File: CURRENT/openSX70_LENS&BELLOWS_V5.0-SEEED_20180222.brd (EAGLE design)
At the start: 95.9 x 27.9 mm, 45 parts, among them Q1 5.8A/30V/35mΩ, Q2 5.8A/30V/35mΩ, U1 ATMEGA328P_TQFP, U3 BH1750FVI-TR, Y1 CSTCE8M00G52Z-R0

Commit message: New board nickname: Len's&Bellows 5.0 (different from Len's & Bellows 4.x): moved Atmega up, and much more little improvements!
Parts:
- moved U1 0.86 mm to (80.9, 16.6)
- moved Q1 0.50 mm to (84.3, 9.59)
- moved R2 0.40 mm to (80.8, 9.46)
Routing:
- net S3: track 12.8 -> 15.4 mm
- net S5: track 15.3 -> 17.9 mm
- net GND: track 15.5 -> 12.9 mm, vias 11 -> 13
- net 3.3V: track 156.5 -> 154.4 mm
- net 100R: track 109.2 -> 107.6 mm
- net S9@2.5V: track 77.1 -> 76.0 mm
- net N$1: track 8.35 -> 7.36 mm
- net S8@2.5V: track 69.1 -> 68.2 mm
- net FF: track 70.3 -> 69.7 mm
- net SOL2: track 90.5 -> 89.9 mm
- net N$4: track 6.09 -> 6.67 mm
- net MOTOR+: track 7.49 -> 6.95 mm
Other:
- board text added: ""Len's & Bellows""
- board text added: "20180222"
- board text added: "layout 5.0"
- board text added: "openSX70 project visit www.openSX70.com version 5.0 "Len's & Bellows" 20170222 by Joaquín de Prada"
- board text removed: ""aladdin-fpc-S""
- board text removed: ""aladdin-fpc-s""
- board text removed: "20180221"
- board text removed: "layout 3.9.8BS"
- board text removed: "openSX70 project visit www.openSX70.com version 3.9.8BS "Aladdin-fpc-S" 20170221 by Joaquín de Prada"

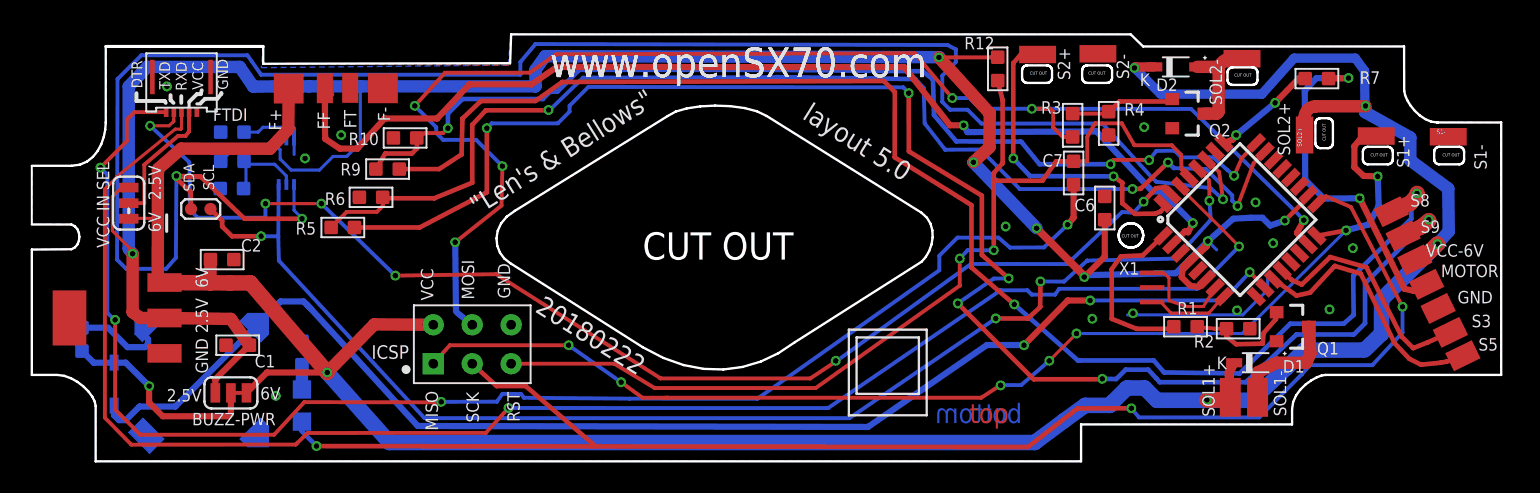
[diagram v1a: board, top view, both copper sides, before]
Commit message: Major folder rearrangement, latest 5.0 Lens-and-Bellows
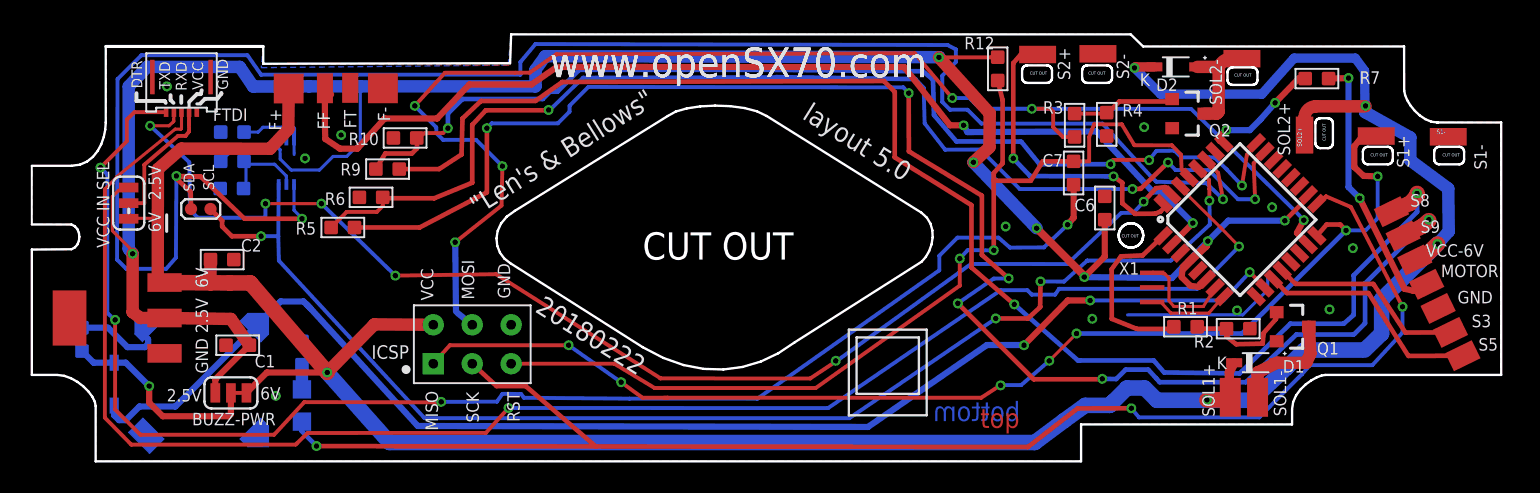
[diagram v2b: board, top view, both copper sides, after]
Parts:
- moved R4 0.14 mm to (72.2, 22.8)
- moved R3 0.13 mm to (70.1, 22.7)
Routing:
- net MOTOR-HEADER: track 22.6 -> 17.6 mm
- net S3: track 15.4 -> 13.0 mm
- net S5: track 17.9 -> 15.8 mm
- net S8@2.5V: track 68.2 -> 69.5 mm
- net 3.3V: track 154.4 -> 153.4 mm
- net MOTOR+: track 6.95 -> 7.81 mm
- net S1: track 77.5 -> 78.2 mm
- net GND: vias 13 -> 11

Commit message: All ready for manufacture!
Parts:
- R15: value 100R -> 0R
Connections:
- new net 0R: U$4.3
- net 100R: no longer U$4.3
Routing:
- net 100R: track 107.6 -> 106.6 mm
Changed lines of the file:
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@@
 <attribute name="VALUE" x="8.525" y="21.932" size="1.27" layer="27"/>
 </element>
-<element name="R15" library="Seeed-Resistor" library_urn="urn:adsk.eagle:library:474" package="R0603" package3d_urn="urn:adsk.eagle:package:32791/1" value="100R" x="5.334" y="8.763" smashed="yes" rot="MR0">
+<element name="R15" library="Seeed-Resistor" library_urn="urn:adsk.eagle:library:474" package="R0603" package3d_urn="urn:adsk.eagle:package:32791/1" value="0R" x="5.334" y="8.763" smashed="yes" rot="MR0">
 <attribute name="MPN" value="RC0603JR-07100RL" x="5.334" y="8.763" size="1.778" layer="28" rot="MR0" display="off"/>
 <attribute name="NAME" x="3.475" y="7.79" size="0.8128" layer="26" font="vector" ratio="20" rot="MR90"/>
@@
 <wire x1="54.01945" y1="4.2799" x2="33.48355" y2="4.28625" width="0.254" layer="16"/>
 <wire x1="33.48355" y1="4.28625" x2="33.16605" y2="4.2926" width="0.254" layer="16"/>
-<contactref element="U$4" pad="3"/>
 <wire x1="11.77925" y1="22.479" x2="11.825" y2="22.52475" width="0.2032" layer="1"/>
-<wire x1="11.825" y1="22.52475" x2="11.825" y2="23.582" width="0.2032" layer="1"/>
 <wire x1="69.088" y1="12.065" x2="78.105" y2="12.065" width="0.254" layer="16"/>
 <wire x1="78.105" y1="12.065" x2="78.77175" y2="12.73175" width="0.254" layer="16"/>
@@
 <wire x1="9.353303125" y1="9.171203125" x2="9.234703125" y2="9.171203125" width="0.4064" layer="16"/>
 </signal>
+<signal name="0R">
+<contactref element="U$4" pad="3"/>
+</signal>
 </signals>
